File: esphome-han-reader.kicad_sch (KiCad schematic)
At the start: 16 parts, among them J1 RJ12, J2 ProgammingPins, Q1 BC817W, SW1 ResetBtn, SW2 FlashBtn, U1 ESP-07, U2 LD1117S33CTR_SOT223

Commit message: feat: Final Rev??
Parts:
- J1: footprint Connector_RJ:RJ12_Amphenol_54601-x06_Horizontal -> Connector_RJ:RJ12_DS1133-S60BPX
- J2: footprint Connector_PinHeader_2.54mm:PinHeader_1x06_P2.54mm_Vertical -> Connector_PinHeader_2.54mm:PinHeader_1x06_P2.54mm_Vertical_NoSilkscreen
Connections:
- net +3V3: now also R2.2, U2.2 (VO); no longer R2.1, U2.3 (VI)
- net +5V: now also U2.3 (VI); no longer U2.2 (VO)
- net ESP-RX: now also R2.1; no longer R2.2
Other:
- moved on the sheet: C1, C2, R2

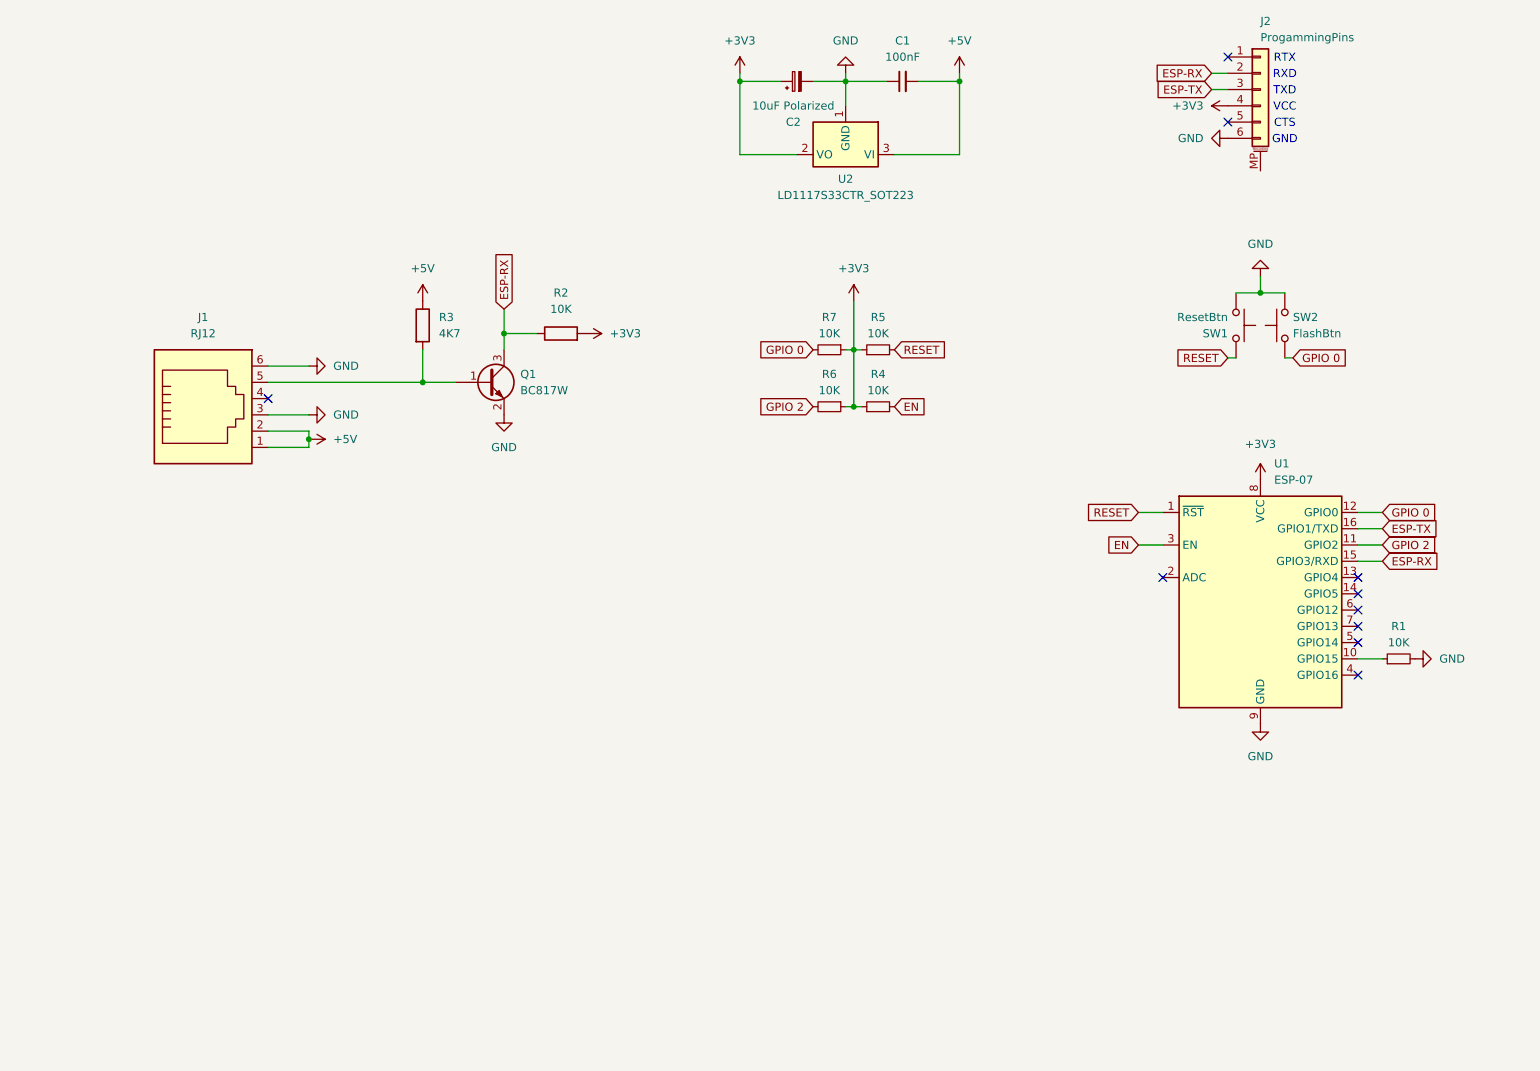
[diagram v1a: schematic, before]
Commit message: feat: new design, new caps and onboard programmer.
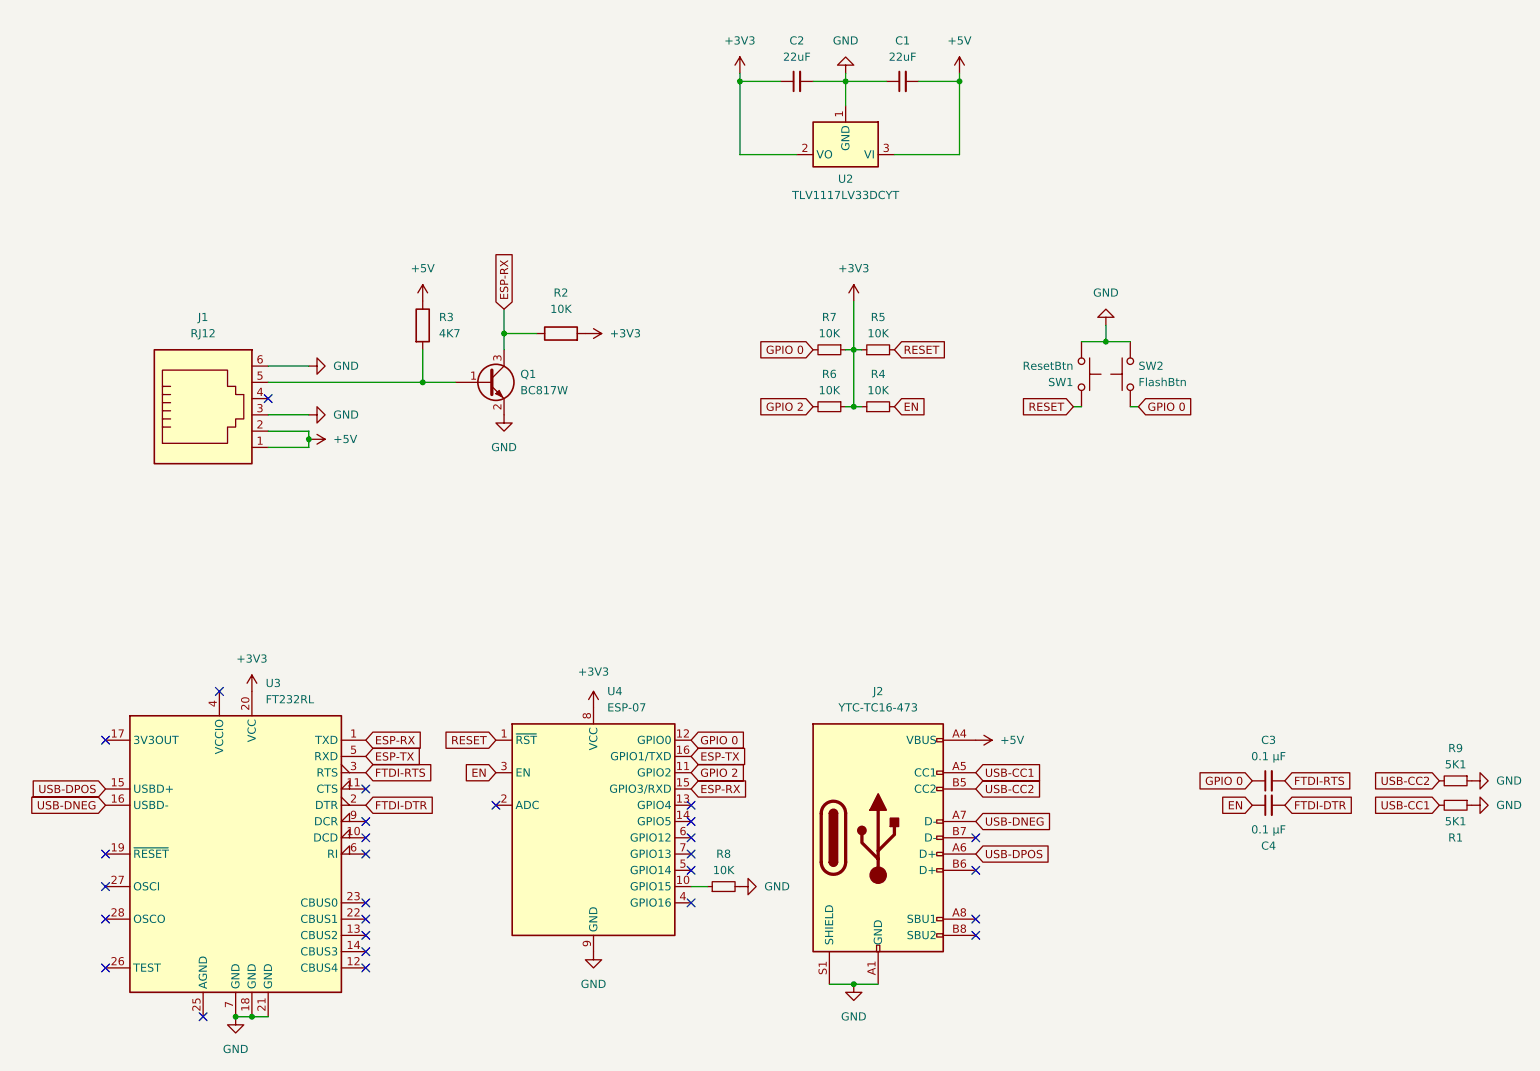
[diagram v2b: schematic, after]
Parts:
- removed C2: 10uF Polarized, Capacitor_Tantalum_SMD:CP_EIA-6032-15_Kemet-U_Pad2.25x2.35mm_HandSolder, symbol Device:C_Polarized_Small
- removed J2: ProgammingPins, Connector_PinHeader_2.54mm:PinHeader_1x06_P2.54mm_Vertical_NoSilkscreen, symbol Connector_Generic_MountingPin:Conn_01x06_MountingPin
- removed U1: ESP-07, RF_Module:ESP-07, symbol RF_Module:ESP-07
- added C2: 22uF, Capacitor_SMD:C_0402_1005Metric, symbol Device:C_Small
- added C3, C4: 0.1 µF, Capacitor_SMD:C_0402_1005Metric, symbol Device:C_Small
- added J2: YTC-TC16-473, Connector_USB:USB_C_Receptacle_XKB_U262-16XN-4BVC11, symbol Connector:USB_C_Receptacle_USB2.0_16P
- added R8: 10K, Resistor_SMD:R_0805_2012Metric_Pad1.20x1.40mm_HandSolder, symbol Device:R_Small
- added R9: 5K1, Resistor_SMD:R_0805_2012Metric_Pad1.20x1.40mm_HandSolder, symbol Device:R_Small
- added U3: FT232RL, Package_SO:SSOP-28_5.3x10.2mm_P0.65mm, symbol Interface_USB:FT232RL
- added U4: ESP-07, RF_Module:ESP-07, symbol RF_Module:ESP-07
- C1: value 100nF -> 22uF; footprint Capacitor_Tantalum_SMD:CP_EIA-6032-15_Kemet-U_Pad2.25x2.35mm_HandSolder -> Capacitor_SMD:C_0402_1005Metric
- R1: value 10K -> 5K1
- U2: value LD1117S33CTR_SOT223 -> TLV1117LV33DCYT
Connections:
- net +3V3: now also C2.1, U3.20 (VCC), U4.8 (VCC)
- net +5V: now also J2.A4 (VBUS), J2.A9 (VBUS), J2.B4 (VBUS), J2.B9 (VBUS)
- net EN: now also C4.1, U4.3 (EN)
- net ESP-RX: now also U3.1 (TXD), U4.15 (GPIO3/RXD)
- net ESP-TX: now also U3.5 (RXD), U4.16 (GPIO1/TXD)
- net GND: now also R1.1, C2.2, J2.A1 (GND), J2.A12 (GND), J2.B1 (GND), J2.B12 (GND), J2.S1 (SHIELD), R8.2, R9.1, U3.18 (GND), U3.21 (GND), U3.7 (GND), U4.9 (GND); no longer R1.2
- net GPIO 0: now also C3.1, U4.12 (GPIO0)
- net GPIO 2: now also U4.11 (GPIO2)
- net RESET: now also U4.1 (~{RST})
- new net: R8.1, U4.10 (GPIO15)
- new net FTDI-DTR: C4.2, U3.2 (DTR)
- new net FTDI-RTS: C3.2, U3.3 (RTS)
- new net USB-CC1: J2.A5 (CC1), R1.2
- new net USB-CC2: J2.B5 (CC2), R9.2
- new net USB-DNEG: J2.A7 (D-), U3.16 (USBD-)
- new net USB-DPOS: J2.A6 (D+), U3.15 (USBD+)
- no-connect marks 10 -> 28
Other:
- note removed: "CTS"
- note removed: "GND"
- note removed: "RTX"
- note removed: "RXD"
- note removed: "TXD"
- note removed: "VCC"
- moved on the sheet: SW1, SW2
